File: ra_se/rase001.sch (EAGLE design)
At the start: 17 parts, among them IC1 74HC14D, X1 MAB5WH, X2 22-23-2041, X3 MAB5WH

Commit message: 11111111111
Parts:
- added R1, R2: 10K, quantum-sensor:R-R1206
- added R9: 3k3, rcl:R-EU_M1206
- added X10, X12, X7, X8, X9: (no value), con-molex:KK-156-2
- added X11, X4, X5, X6: (no value), con-molex:KK-156-3
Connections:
- removed net UART1_RX: OK1.VO, R4.1, U$1.PA10
- new net ENC0_SH: IC1D.O
- new net ENC1_SH: IC1E.O
- new net INMI: OK1.VO, R4.1
- new net INMI_SH: IC1C.O, X5-1.S, X6-1.S
- new net MAX_O: U$2.RO, X6-3.S
- new net N$10: U$1.PA10, X6-2.S
- new net N$11: U$2.DE, U$2.RE, X4-2.S
- new net N$12: R9.2, U$1.PC13_LED1
- new net N$3: IC1B.O, IC1C.I
- new net N$7: R8.2, X5-2.S
- new net N$8: R9.1, X12-2.S
- net BTTN_GLOBALSTART: now also X9-1.S
- net BTTN_GLOBALSTOP: now also X10-1.S
- net BTTN_START_REQST: now also X8-1.S
- net ENCODER0: now also R1.2, X11-1.S; no longer U$1.PB9
- net ENCODER1: now also R2.2, X11-2.S; no longer U$1.PB8
- net GND: now also X10-2.S, X11-3.S, X4-3.S, X7-2.S, X8-2.S, X9-2.S
- net SWITCH_EXTINT: now also X7-1.S
- net UART2_TX: now also X5-3.S; no longer R8.2
- net VCC_5V: now also R1.1, R2.1, X12-1.S, X4-1.S; no longer U$2.DE, U$2.RE

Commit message: something added?
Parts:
- added X13: (no value), con-molex:KK-156-2
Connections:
- new net BTTN_STOP_REQST: U$1.PB0, X13-1.S
- net ENC0_SH: now also U$1.PB9
- net ENC1_SH: now also U$1.PB8
- net GND: now also X13-2.S
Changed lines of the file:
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@@
 <?xml version="1.0" encoding="utf-8"?>
 <!DOCTYPE eagle SYSTEM "eagle.dtd">
-<eagle version="7.1.0">
+<eagle version="8.0.1">
 <drawing>
 <settings>
@@
 <setting verticaltext="up"/>
 </settings>
-<grid distance="0.1" unitdist="inch" unit="inch" style="lines" multiple="1" display="yes" altdistance="0.01" altunitdist="inch" altunit="inch"/>
+<grid distance="0.1" unitdist="inch" unit="inch" style="lines" multiple="1" display="no" altdistance="0.01" altunitdist="inch" altunit="inch"/>
 <layers>
 <layer number="1" name="Top" color="4" fill="1" visible="no" active="no"/>
@@
 <part name="R9" library="rcl" deviceset="R-EU_" device="M1206" value="3k3"/>
 <part name="P+11" library="supply1" deviceset="VCC" device="" value="VCC_5V"/>
+<part name="X13" library="con-molex" deviceset="KK-156-2" device=""/>
+<part name="GND12" library="supply1" deviceset="GND" device=""/>
 </parts>
 <sheets>
@@
 <instance part="R9" gate="G$1" x="30.48" y="119.38" rot="R180"/>
 <instance part="P+11" gate="VCC" x="33.02" y="129.54"/>
+<instance part="X13" gate="-1" x="287.02" y="68.58"/>
+<instance part="X13" gate="-2" x="287.02" y="63.5"/>
+<instance part="GND12" gate="1" x="281.94" y="58.42"/>
 </instances>
 <busses>
@@
 <wire x1="281.94" y1="127" x2="284.48" y2="127" width="0.1524" layer="91"/>
 </segment>
+<segment>
+<pinref part="GND12" gate="1" pin="GND"/>
+<wire x1="281.94" y1="60.96" x2="281.94" y2="63.5" width="0.1524" layer="91"/>
+<pinref part="X13" gate="-2" pin="S"/>
+<wire x1="281.94" y1="63.5" x2="284.48" y2="63.5" width="0.1524" layer="91"/>
+</segment>
 </net>
 <net name="VCC_5V" class="0">
@@
 <wire x1="76.2" y1="99.06" x2="83.82" y2="99.06" width="0.1524" layer="91"/>
 <label x="83.82" y="99.06" size="1.27" layer="95" xref="yes"/>
+<pinref part="U$1" gate="G$1" pin="PB9"/>
 </segment>
 </net>
@@
 <wire x1="76.2" y1="96.52" x2="83.82" y2="96.52" width="0.1524" layer="91"/>
 <label x="83.82" y="96.52" size="1.27" layer="95" xref="yes"/>
+<pinref part="U$1" gate="G$1" pin="PB8"/>
 </segment>
 </net>
@@
 </segment>
 </net>
+<net name="BTTN_STOP_REQST" class="0">
+<segment>
+<pinref part="U$1" gate="G$1" pin="PB0"/>
+<wire x1="22.86" y1="76.2" x2="12.7" y2="76.2" width="0.1524" layer="91"/>
+<label x="12.7" y="76.2" size="1.27" layer="95" rot="R180" xref="yes"/>
+</segment>
+<segment>
+<wire x1="284.48" y1="68.58" x2="274.32" y2="68.58" width="0.1524" layer="91"/>
+<label x="274.32" y="68.58" size="1.27" layer="95" rot="R180" xref="yes"/>
+<pinref part="X13" gate="-1" pin="S"/>
+</segment>
+</net>

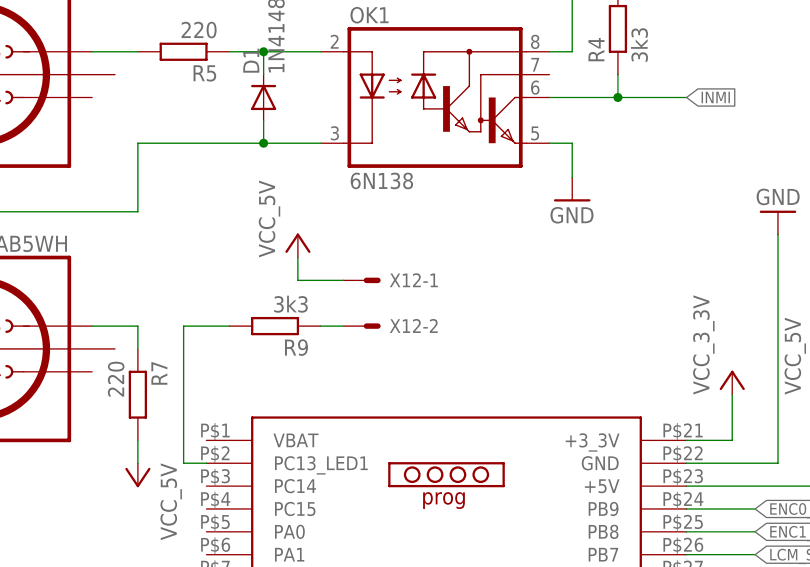
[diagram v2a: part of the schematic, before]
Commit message: led named
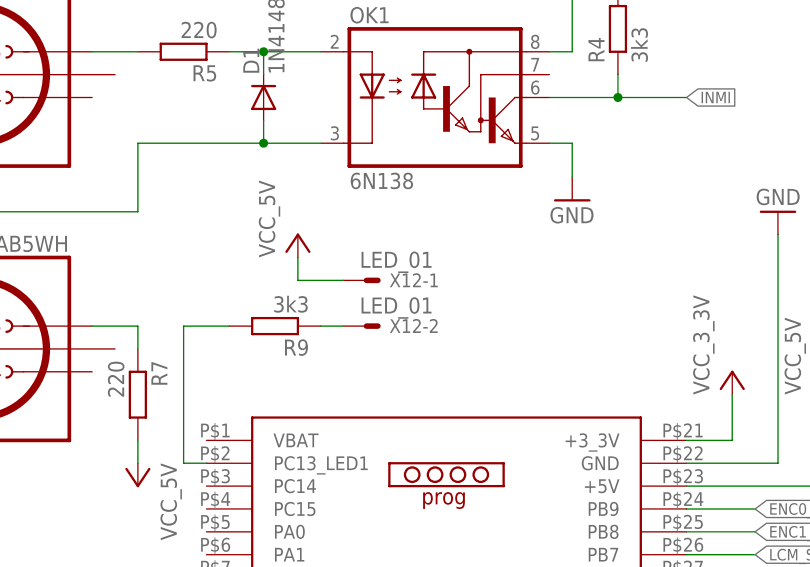
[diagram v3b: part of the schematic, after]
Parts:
- X12: value (none) -> LED_01
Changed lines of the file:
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@@
 <part name="GND11" library="supply1" deviceset="GND" device=""/>
 <part name="X11" library="con-molex" deviceset="KK-156-3" device=""/>
-<part name="X12" library="con-molex" deviceset="KK-156-2" device=""/>
+<part name="X12" library="con-molex" deviceset="KK-156-2" device="" value="LED_01"/>
 <part name="R9" library="rcl" deviceset="R-EU_" device="M1206" value="3k3"/>
 <part name="P+11" library="supply1" deviceset="VCC" device="" value="VCC_5V"/>
